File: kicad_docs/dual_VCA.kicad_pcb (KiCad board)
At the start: 2 copper layers, 45.7 x 99.1 mm, 68 parts, among them J1 signal_in_1, J2 CV_in_1, J3 signal_in_2, J4 CV_in_2, J5 signal_out_1, J6 signal_out_2, J7 power_input, J8 Conn_01x06, J9 Conn_01x06, U1 SSM2164, U2 TL072, U3 TL072, U4 TL072, U5 TL072, U6 MAX6035xxUR50

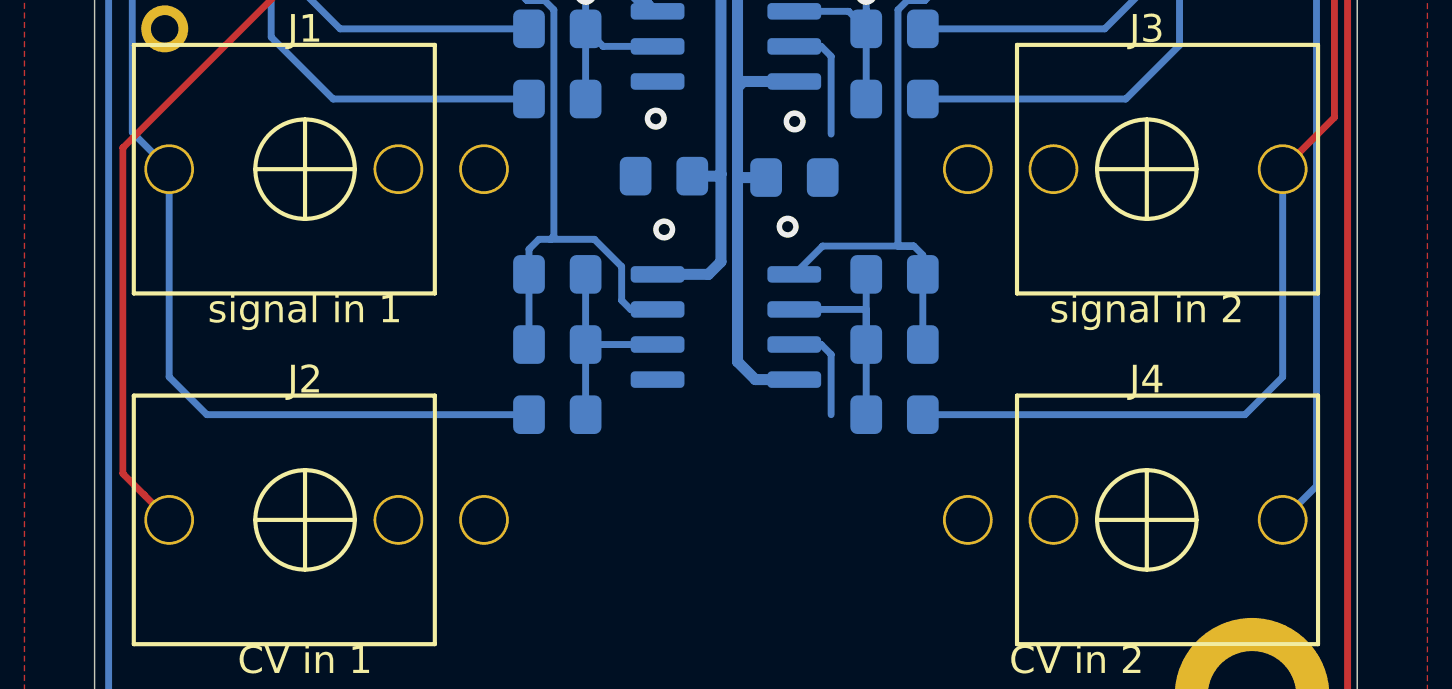
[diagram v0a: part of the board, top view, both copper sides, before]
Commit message: add AC/DC coupling caps and jumper
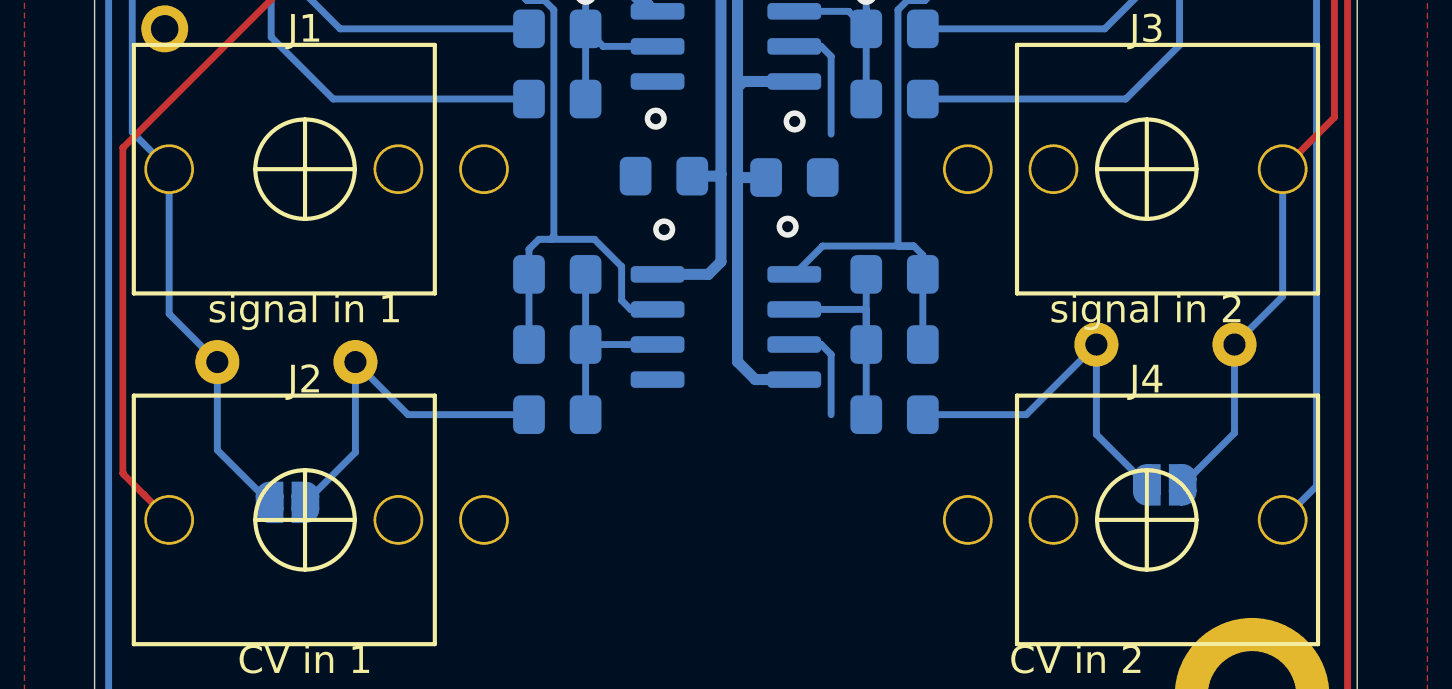
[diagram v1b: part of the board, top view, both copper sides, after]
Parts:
- added C24: 470nF, Capacitor_THT:C_Rect_L7.2mm_W3.5mm_P5.00mm_FKS2_FKP2_MKS2_MKP2, B.Cu at (80.6, 149.2)
- added C25: 470nF, Capacitor_THT:C_Rect_L7.2mm_W3.5mm_P5.00mm_FKS2_FKP2_MKS2_MKP2, B.Cu at (107.4, 148.6)
- added JP1: AC/DC coupling, Jumper:SolderJumper-2_P1.3mm_Open_RoundedPad1.0x1.5mm, B.Cu at (78.1, 154.3)
- added JP2: AC/DC coupling, Jumper:SolderJumper-2_P1.3mm_Open_RoundedPad1.0x1.5mm, B.Cu at (109.9, 153.7)
- C2, C7: value 100pF -> 22pF
- R14, R15, R7, R8: value 30k -> 100k
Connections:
- R14 pad 2: /signal_in_1 -> /VCA_1/VCA_1_signal_v_in
- R7 pad 2: /signal_in_2 -> /VCA_2/VCA_2_signal_v_in
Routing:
- net /VCA_2/VCA_2_signal_v_in: track 0.00 -> 13.2 mm
- net /VCA_1/VCA_1_signal_v_in: track 0.00 -> 12.9 mm
- net /signal_in_2: track 106.2 -> 98.0 mm
- net /signal_in_1: track 42.1 -> 34.6 mm
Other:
- board text added: "bridge for DC"

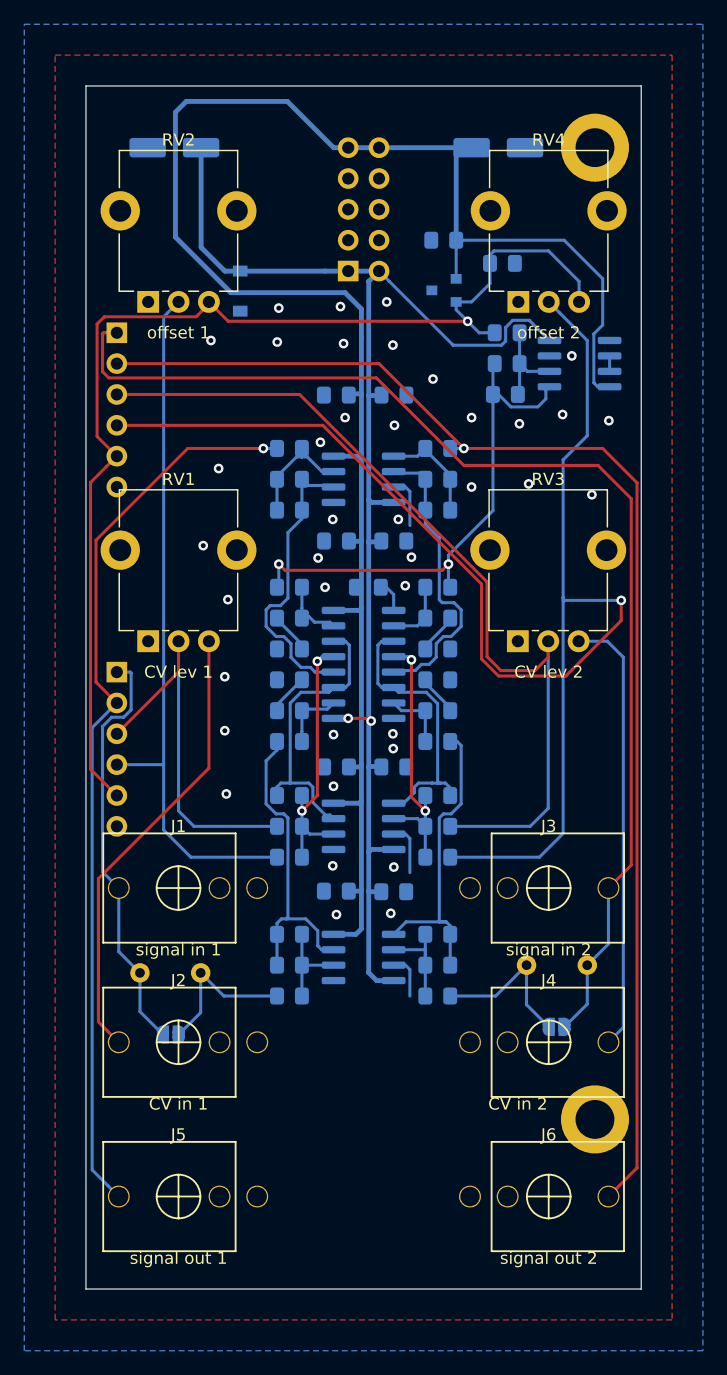
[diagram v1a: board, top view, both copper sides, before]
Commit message: add values to r's, add r's to CV circuit
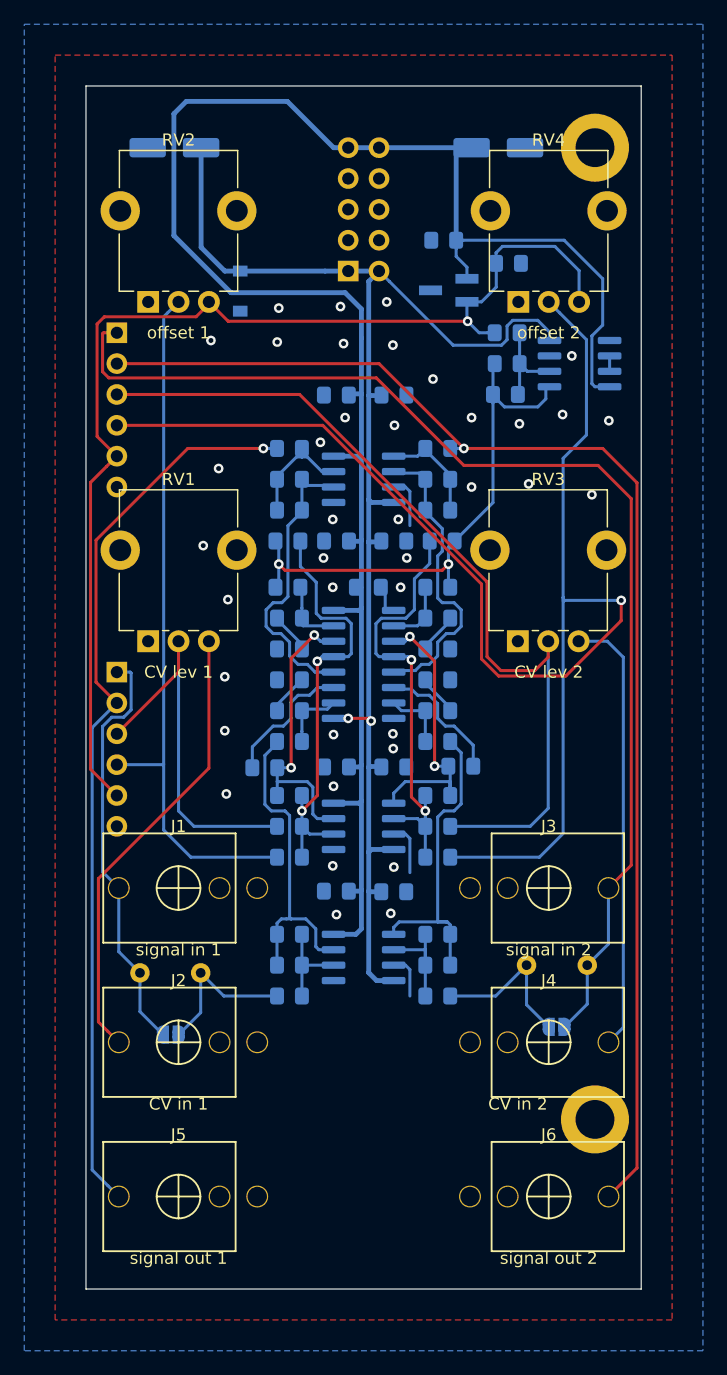
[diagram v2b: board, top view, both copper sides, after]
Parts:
- added R24: 10M, Resistor_SMD:R_0805_2012Metric_Pad1.15x1.40mm_HandSolder, B.Cu at (87.7, 113.7)
- added R25: 4k7, Resistor_SMD:R_0805_2012Metric_Pad1.15x1.40mm_HandSolder, B.Cu at (85.8, 132.3)
- added R26: 10M, Resistor_SMD:R_0805_2012Metric_Pad1.15x1.40mm_HandSolder, B.Cu at (100.4, 113.7)
- added R27: 4k7, Resistor_SMD:R_0805_2012Metric_Pad1.15x1.40mm_HandSolder, B.Cu at (102.0, 132.2)
- R1, R2, R3, R4: value R -> 100k
- R11, R18: value ??? -> 100k
- U6: footprint Package_TO_SOT_SMD:SOT-23 -> Package_TO_SOT_SMD:SOT-23_Handsoldering
- moved C12 0.50 mm to (105.9, 90.8)
- moved U6 0.39 mm to (101.0, 93.0)
- moved R18 0.13 mm to (87.7, 117.5)
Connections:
- U1 pad 11: Net-(C6-Pad1) -> Net-(R25-Pad1)
- U1 pad 6: Net-(C1-Pad1) -> Net-(R27-Pad1)
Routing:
- net /VCA_2/VCA_2_CV_summing_node_i_in: track 22.4 -> 36.3 mm
- net /VCA_1/VCA_1_CV_summing_node_i_in: track 22.4 -> 36.2 mm
- net Net-(R27-Pad1): track 0.00 -> 11.0 mm
- net Net-(R25-Pad1): track 0.00 -> 10.5 mm
- net -5VA: track 42.5 -> 44.7 mm
- net +12V: track 153.2 -> 154.6 mm
- net Net-(C7-Pad1): track 26.2 -> 26.7 mm
- net Net-(C6-Pad1): track 24.2 -> 24.5 mm, vias 0 -> 2
- net Net-(C1-Pad1): track 22.8 -> 23.0 mm, vias 0 -> 2
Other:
- board text added: "bridge for DC ch 1"
- board text added: "bridge for DC ch 2"
- board text removed: "bridge for DC"

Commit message: add github url to pcb silkscreen
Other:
- board text added: "github.com/JordanAceto/Dual_2164_VCA rev 1 2020-02-23"
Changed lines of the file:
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@@
   (general
     (thickness 1.6)
-    (drawings 33)
+    (drawings 34)
     (tracks 520)
     (zones 0)
@@
     )
   )
+  (gr_text "github.com/JordanAceto/Dual_2164_VCA\nrev 1\n2020-02-23" (at 115.951 171.831) (layer B.SilkS)
+    (effects (font (size 1 1) (thickness 0.15)) (justify left mirror))
+  )
   (gr_text "bridge\nfor DC\nch 2" (at 109.855 156.845) (layer B.SilkS)
